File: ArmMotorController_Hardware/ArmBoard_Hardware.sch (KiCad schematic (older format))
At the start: 116 parts, among them Q1 Q_NMOS_GSD, Q2 Q_NMOS_GSD, U1 TM4C129E_Launchpad, U2 MAX_3232, U3 OKI, U4 OKI, U5 VNH5019A_E, U6 MAX_3232

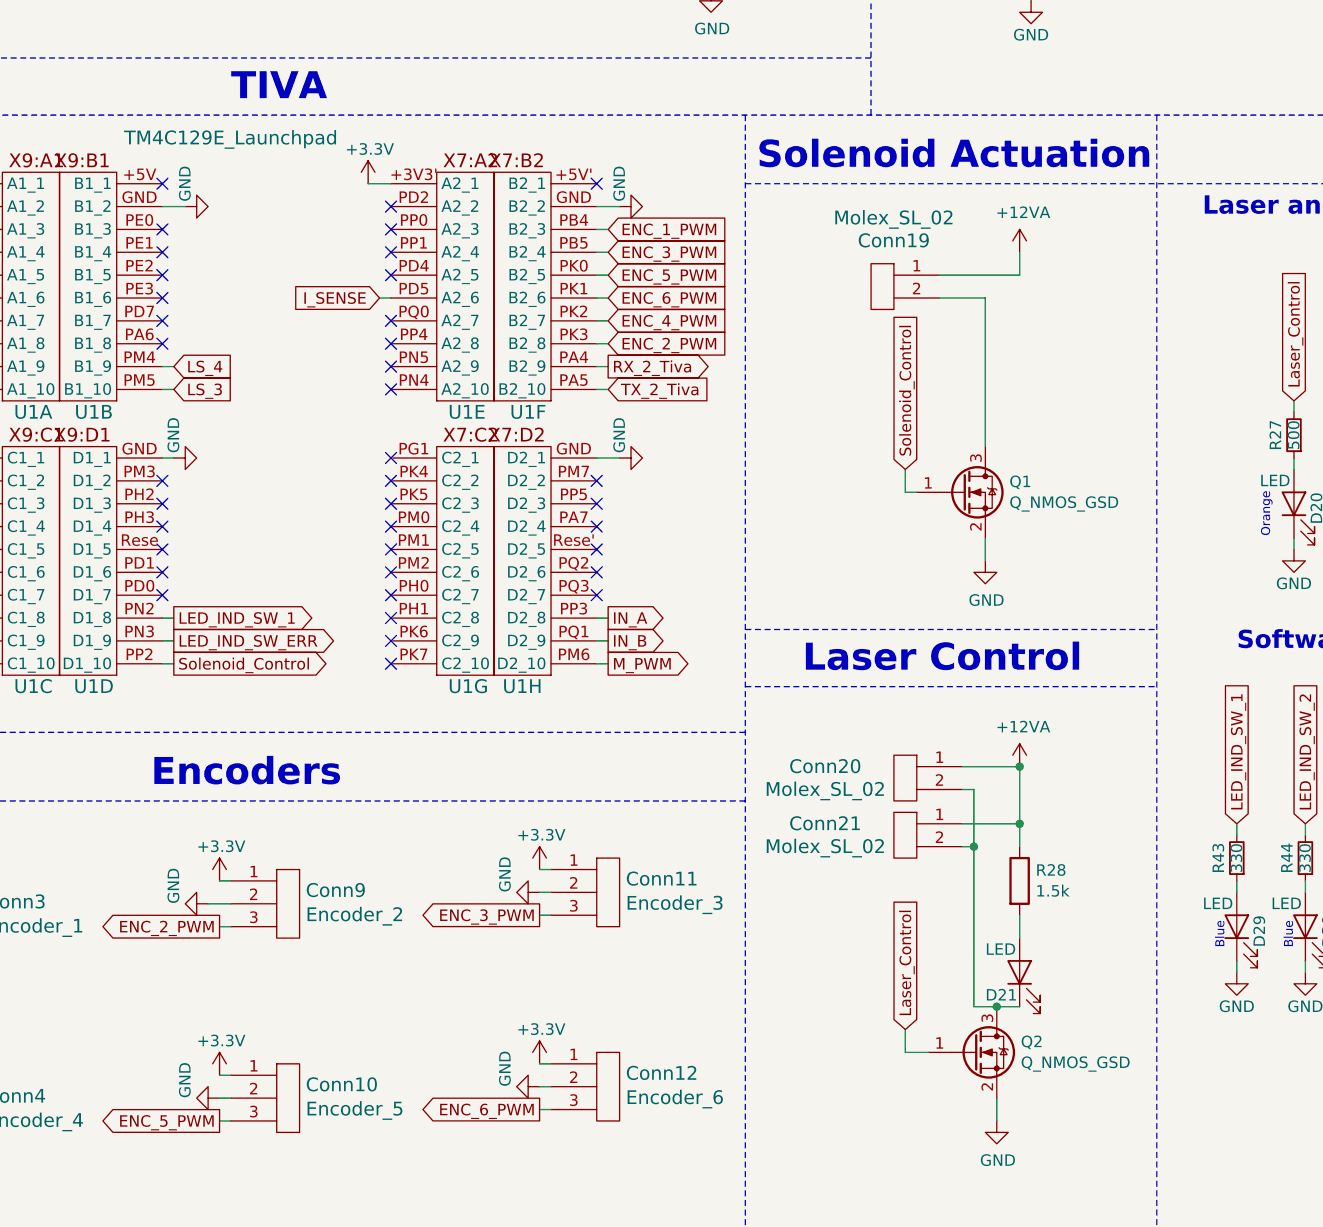
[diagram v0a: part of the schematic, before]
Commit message: Reducing Electrical Leads bitching potential
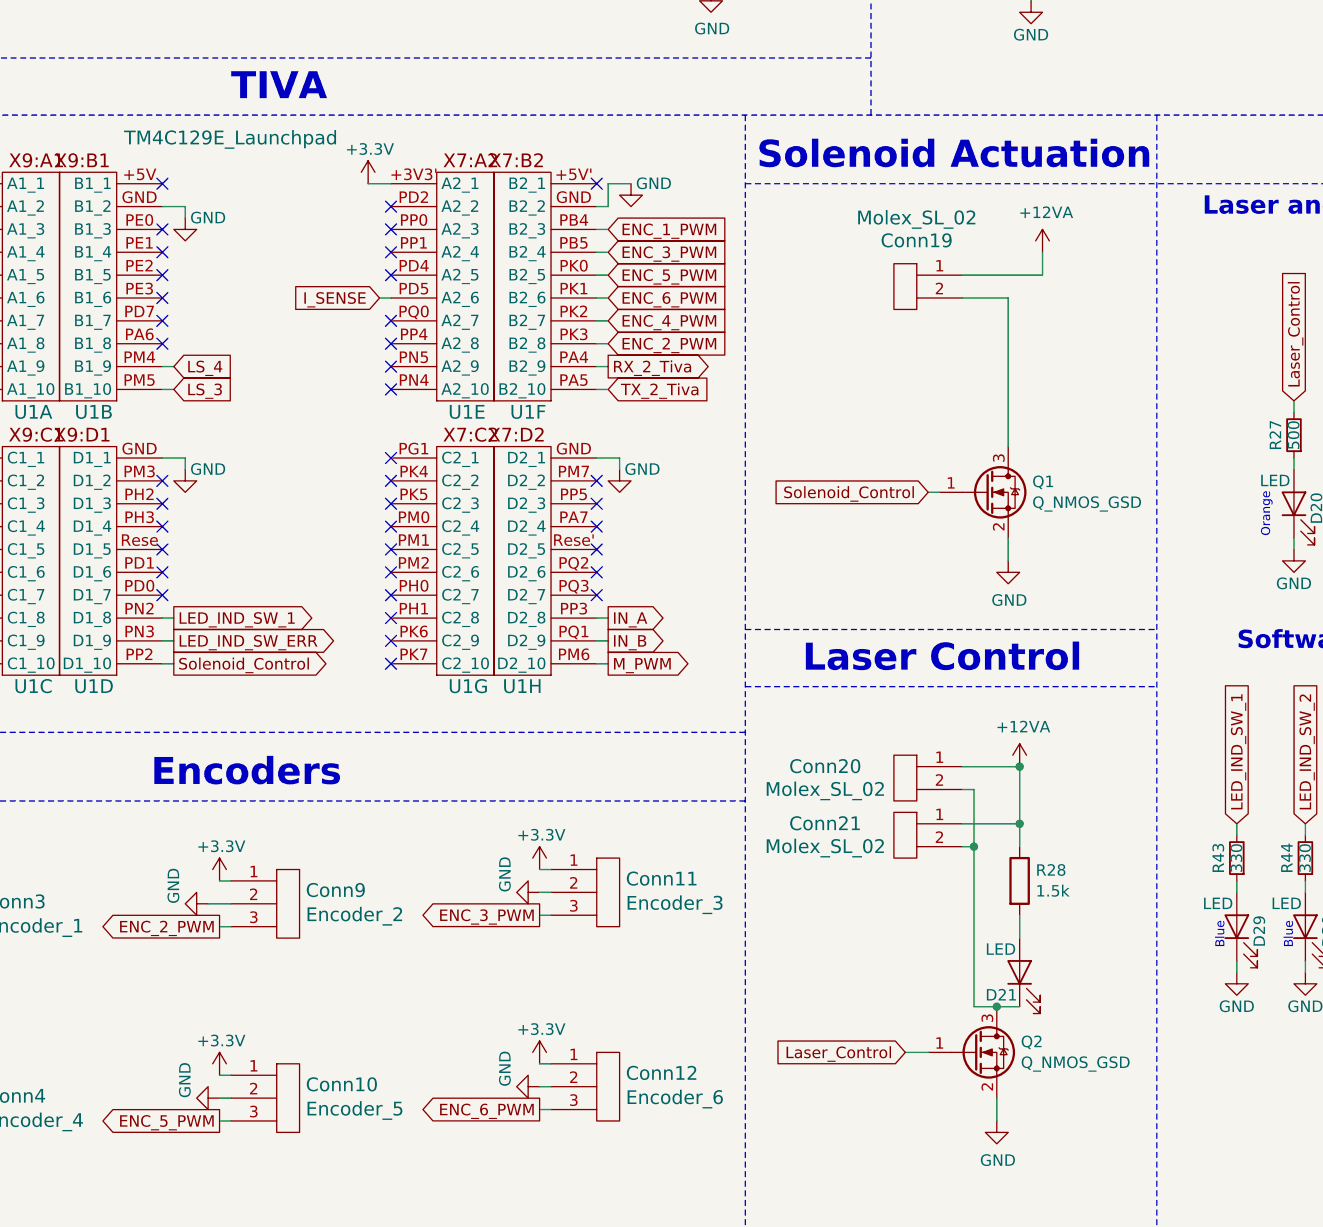
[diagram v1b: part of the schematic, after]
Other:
- moved on the sheet: Conn19, Q1
